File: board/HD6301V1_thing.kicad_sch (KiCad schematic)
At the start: 42 parts, among them J1 KMDGX-6S-BS, J2 ps2_i2c, J3 P1_connector, J4 memmap_i2c, J5 8bit_thing_bus_connector, J6 USB_B_Micro, J7 prog_LED, J8 pwr_LED, SW1 Reset, SW2 Banking, U1 APX811-46, U2 74LVC2G08, U3 SLG46826G, U4 HD6301V1, U5 SLG46826G, U6 74HCT573, U7 IS62C256AL, U8 SST39SF010, X1 CXO_DIP8

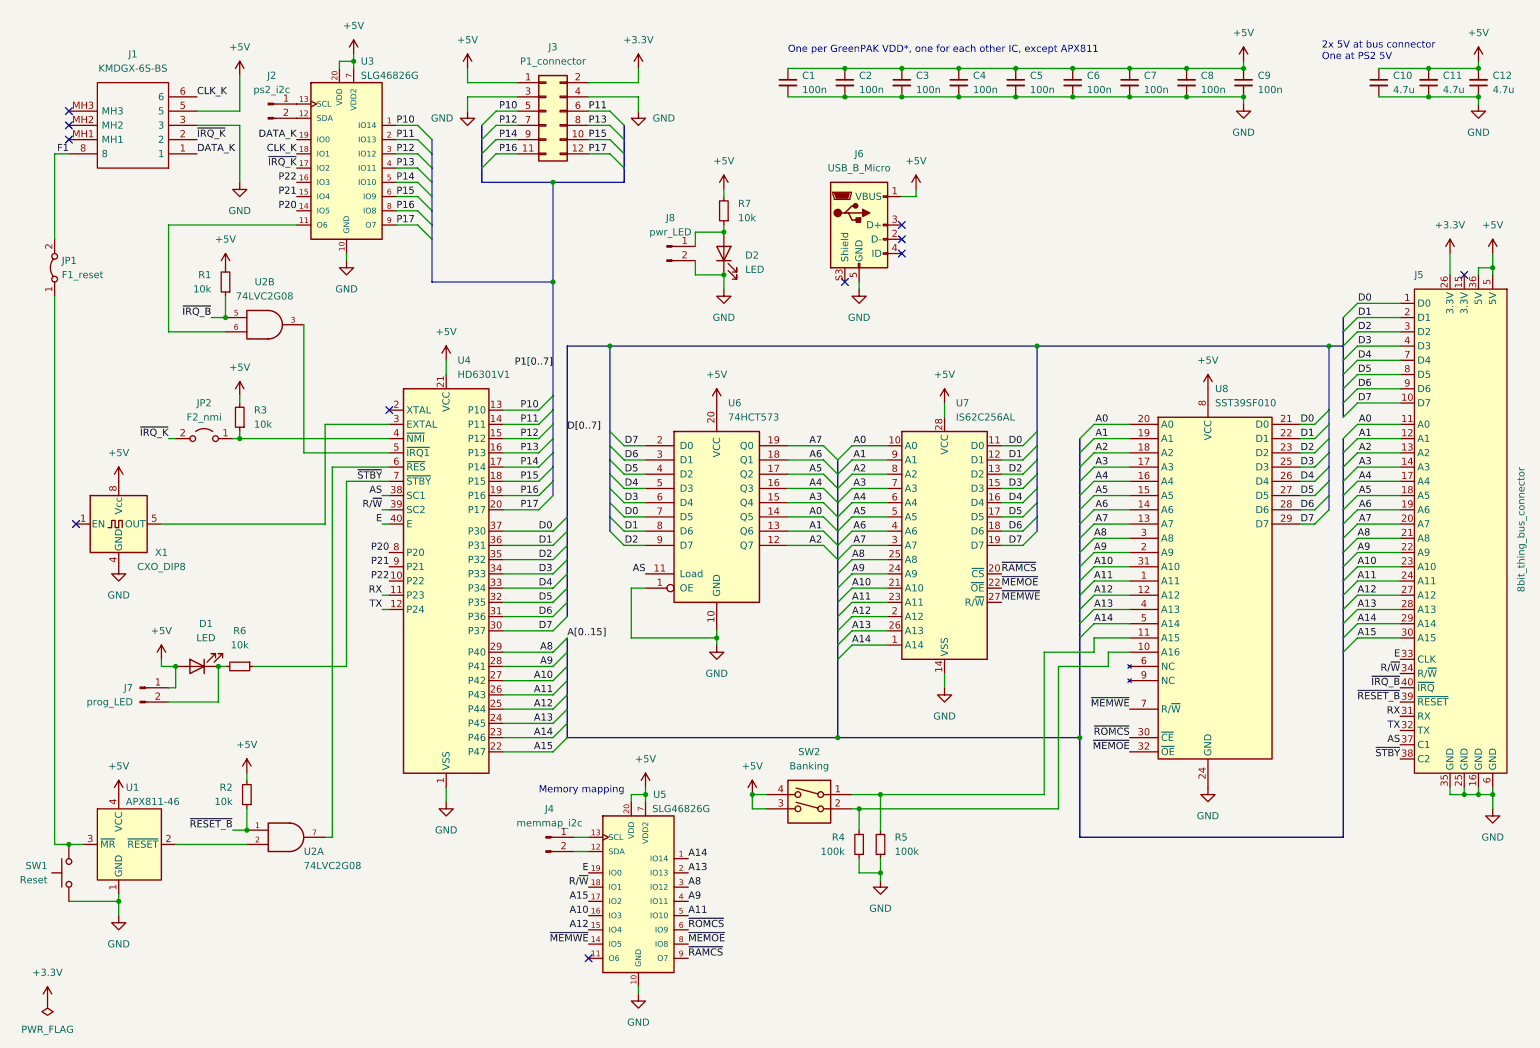
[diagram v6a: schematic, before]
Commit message: Update schematic for new Greenpak symbol and some small changes to the PCB
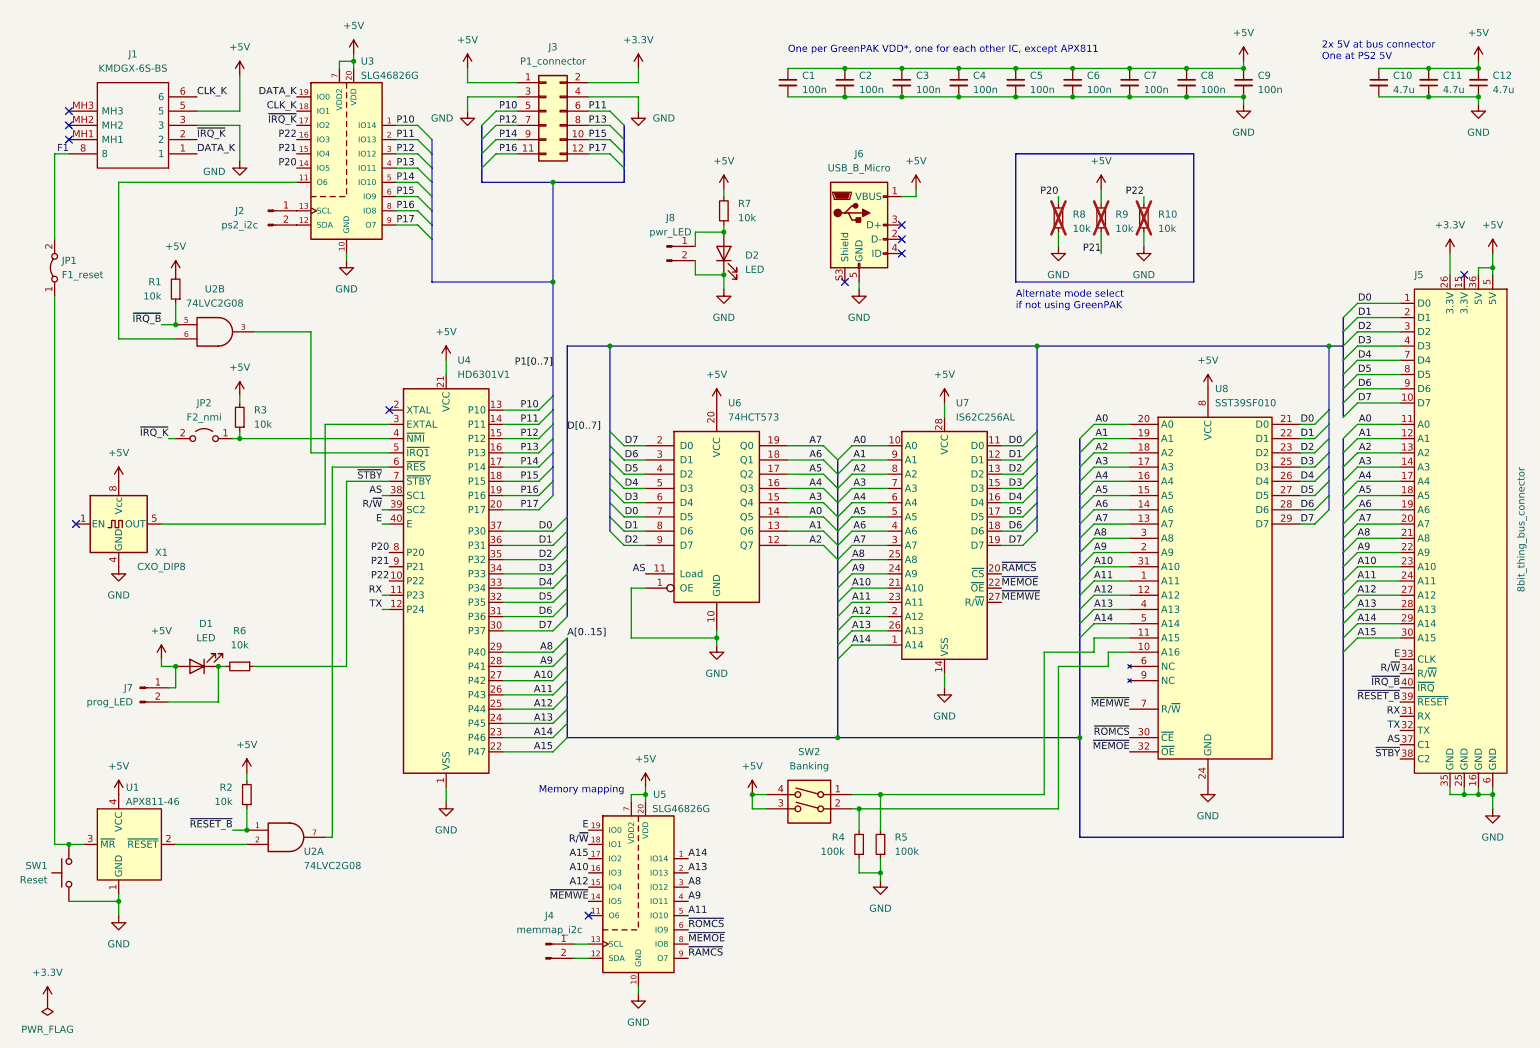
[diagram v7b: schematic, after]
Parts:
- added R10, R8, R9: 10k, Resistor_SMD:R_0805_2012Metric_Pad1.20x1.40mm_HandSolder, symbol Device:R_Small
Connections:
- net +5V: now also R9.2
- net GND: now also R10.1, R8.1
- net P20: now also R8.2
- net P21: now also R9.1
- net P22: now also R10.2
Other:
- note added: "Alternate mode select if not using GreenPAK"
- moved on the sheet: J2, J4, R1, U2B

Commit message: Some small improvements to HD6301 PCB
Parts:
- U3, U5: footprint imported_footprints:SOP65P640X120-20N -> SOP65P640X120-20N
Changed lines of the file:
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@@
     )
   )
-  (symbol (lib_name "SLG46826G_1") (lib_id "imported_symbols:SLG46826G") (at 71.12 40.64 0) (unit 1)
+  (symbol (lib_id "imported_symbols:SLG46826G") (at 71.12 40.64 0) (unit 1)
     (in_bom yes) (on_board yes) (dnp no)
     (property "Reference" "U3" (at 73.66 22.86 0)
@@
       (effects (font (size 1.27 1.27)) (justify left))
     )
-    (property "Footprint" "imported_footprints:SOP65P640X120-20N" (at 91.44 63.5 0)
+    (property "Footprint" "SOP65P640X120-20N" (at 91.44 63.5 0)
       (effects (font (size 1.27 1.27)) (justify bottom) hide)
     )
@@
       (effects (font (size 1.27 1.27)))
     )
-    (property "Footprint" "imported_footprints:SOP65P640X120-20N" (at 123.19 171.45 0)
+    (property "Footprint" "SOP65P640X120-20N" (at 123.19 171.45 0)
       (effects (font (size 1.27 1.27)) (justify bottom) hide)
     )
